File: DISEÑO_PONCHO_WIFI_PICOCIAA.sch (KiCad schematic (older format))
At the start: 11 parts, among them P1 MOUNT_HOLE, P2 MOUNT_HOLE, U1 ESP-12E

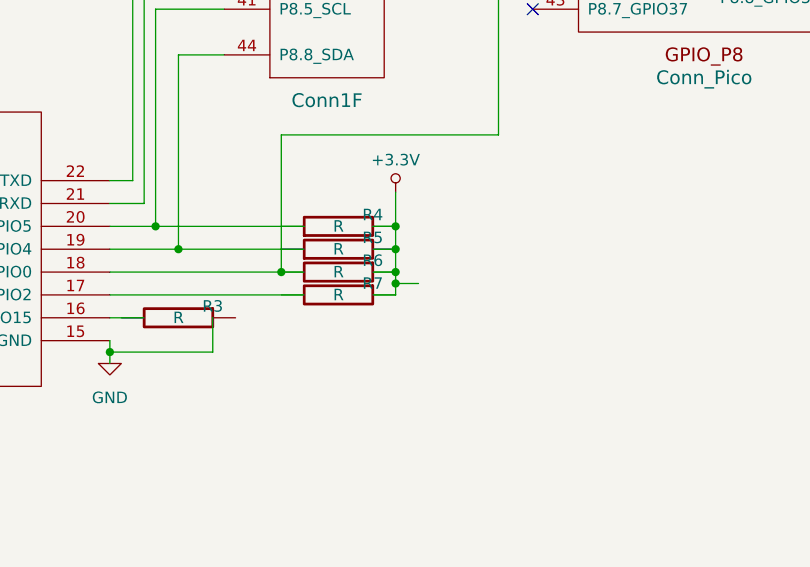
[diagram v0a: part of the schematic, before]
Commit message: Comentarios DB
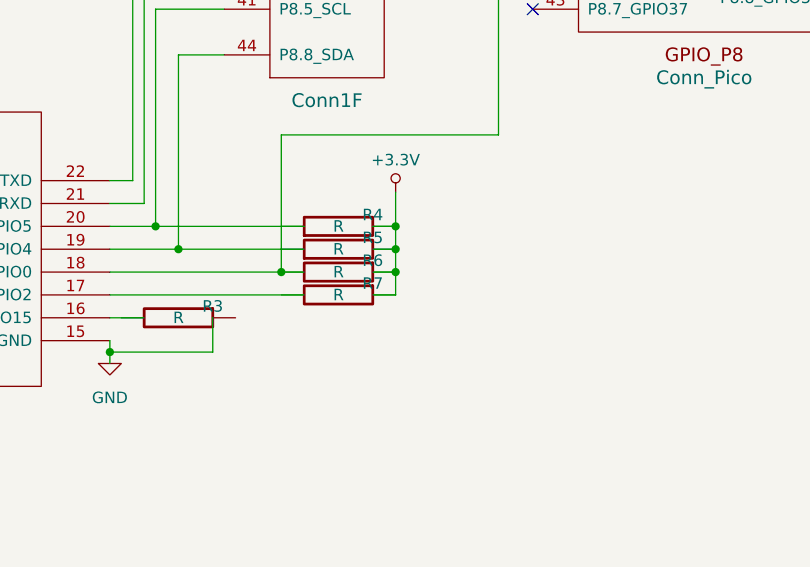
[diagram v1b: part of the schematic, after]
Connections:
- wire segments 52 -> 51
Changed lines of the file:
@@
 EESchema Schematic File Version 2
 LIBS:power
-LIBS:device
-LIBS:transistors
-LIBS:conn
-LIBS:linear
-LIBS:regul
-LIBS:74xx
-LIBS:cmos4000
-LIBS:adc-dac
-LIBS:memory
-LIBS:xilinx
-LIBS:microcontrollers
-LIBS:dsp
-LIBS:microchip
-LIBS:analog_switches
-LIBS:motorola
-LIBS:texas
-LIBS:intel
-LIBS:audio
-LIBS:interface
-LIBS:digital-audio
-LIBS:philips
-LIBS:display
-LIBS:cypress
-LIBS:siliconi
-LIBS:opto
-LIBS:atmel
-LIBS:contrib
-LIBS:valves
-LIBS:ESP8266
-LIBS:logo
-LIBS:poncho_eth
-LIBS:PonchoPLC-cache
-LIBS:Poncho_Esqueleto
 LIBS:DISEÑO_PONCHO_WIFI_PICOCIAA-cache
 EELAYER 25 0
@@
 	7050 4950 6600 4950
 Connection ~ 6600 4950
-Wire Wire Line
-	7850 4650 7950 4650
-Connection ~ 7850 4650
 Connection ~ 6900 4500
 Connection ~ 6800 4400

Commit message: Footprints locales
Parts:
- Conn1: footprint pico_ciaa_ponchos:Conn_Pico_Ciaa -> Poncho_wifi:Conn_Pico_Ciaa
- P1, P2: footprint footprints:PIN_ARRAY_1 -> Poncho_wifi:PIN_ARRAY_1
- R1, R2, R3, R4, R5, R6, R7: footprint Resistors_SMD:R_0805_HandSoldering -> Poncho_wifi:R_0805_HandSoldering
- U1: footprint pico_ciaa_ponchos:ESP-12E -> Poncho_wifi:ESP-12E
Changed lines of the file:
@@
 F 0 "U1" H 5700 4400 50  0000 C CNN
 F 1 "ESP-12E" H 5700 4600 50  0000 C CNN
-F 2 "pico_ciaa_ponchos:ESP-12E" H 5700 4500 50  0001 C CNN
+F 2 "Poncho_wifi:ESP-12E" H 5700 4500 50  0001 C CNN
 F 3 "" H 5700 4500 50  0001 C CNN
 	1    5700 4500
@@
 F 0 "R1" V 4400 4350 50  0000 C CNN
 F 1 "R" V 4450 4200 50  0000 C CNN
-F 2 "Resistors_SMD:R_0805_HandSoldering" V 4380 4200 50  0001 C CNN
+F 2 "Poncho_wifi:R_0805_HandSoldering" V 4380 4200 50  0001 C CNN
 F 3 "" H 4450 4200 50  0000 C CNN
 	1    4450 4200
@@
 F 0 "R2" V 4400 4550 50  0000 C CNN
 F 1 "R" V 4450 4400 50  0000 C CNN
-F 2 "Resistors_SMD:R_0805_HandSoldering" V 4380 4400 50  0001 C CNN
+F 2 "Poncho_wifi:R_0805_HandSoldering" V 4380 4400 50  0001 C CNN
 F 3 "" H 4450 4400 50  0000 C CNN
 	1    4450 4400
@@
 F 0 "R6" V 7550 4750 50  0000 C CNN
 F 1 "R" V 7600 4600 50  0000 C CNN
-F 2 "Resistors_SMD:R_0805_HandSoldering" V 7530 4600 50  0001 C CNN
+F 2 "Poncho_wifi:R_0805_HandSoldering" V 7530 4600 50  0001 C CNN
 F 3 "" H 7600 4600 50  0000 C CNN
 	1    7600 4600
@@
 F 0 "R7" V 7550 4850 50  0000 C CNN
 F 1 "R" V 7600 4700 50  0000 C CNN
-F 2 "Resistors_SMD:R_0805_HandSoldering" V 7530 4700 50  0001 C CNN
+F 2 "Poncho_wifi:R_0805_HandSoldering" V 7530 4700 50  0001 C CNN
 F 3 "" H 7600 4700 50  0000 C CNN
 	1    7600 4700
@@
 F 0 "R3" V 6850 4950 50  0000 C CNN
 F 1 "R" V 6900 4800 50  0000 C CNN
-F 2 "Resistors_SMD:R_0805_HandSoldering" V 6830 4800 50  0001 C CNN
+F 2 "Poncho_wifi:R_0805_HandSoldering" V 6830 4800 50  0001 C CNN
 F 3 "" H 6900 4800 50  0000 C CNN
 	1    6900 4800
@@
 F 0 "R4" V 7650 4250 50  0000 C CNN
 F 1 "R" V 7600 4400 50  0000 C CNN
-F 2 "Resistors_SMD:R_0805_HandSoldering" V 7530 4400 50  0001 C CNN
+F 2 "Poncho_wifi:R_0805_HandSoldering" V 7530 4400 50  0001 C CNN
 F 3 "" H 7600 4400 50  0000 C CNN
 	1    7600 4400
@@
 F 0 "R5" V 7650 4350 50  0000 C CNN
 F 1 "R" V 7600 4500 50  0000 C CNN
-F 2 "Resistors_SMD:R_0805_HandSoldering" V 7530 4500 50  0001 C CNN
+F 2 "Poncho_wifi:R_0805_HandSoldering" V 7530 4500 50  0001 C CNN
 F 3 "" H 7600 4500 50  0000 C CNN
 	1    7600 4500
@@
 F 0 "P1" H 2100 6900 50  0000 C CNN
 F 1 "MOUNT_HOLE" V 2200 6800 50  0000 C CNN
-F 2 "footprints:PIN_ARRAY_1" H 2100 6800 50  0001 C CNN
+F 2 "Poncho_wifi:PIN_ARRAY_1" H 2100 6800 50  0001 C CNN
 F 3 "" H 2100 6800 50  0000 C CNN
 	1    2100 6800
@@
 F 0 "P2" H 2100 7450 50  0000 C CNN
 F 1 "MOUNT_HOLE" V 2200 7350 50  0000 C CNN
-F 2 "footprints:PIN_ARRAY_1" H 2100 7350 50  0001 C CNN
+F 2 "Poncho_wifi:PIN_ARRAY_1" H 2100 7350 50  0001 C CNN
 F 3 "" H 2100 7350 50  0000 C CNN
 	1    2100 7350
@@
 F 0 "Conn1" H 3100 4950 60  0000 C CNN
 F 1 "Conn_Pico" H 3100 3850 60  0000 C CNN
-F 2 "pico_ciaa_ponchos:Conn_Pico_Ciaa" H 3250 4400 60  0001 C CNN
+F 2 "Poncho_wifi:Conn_Pico_Ciaa" H 3250 4400 60  0001 C CNN
 F 3 "" H 3250 4400 60  0000 C CNN
 F 4 "Value" H 3100 4450 60  0001 C CNN "Digikey#"
@@
 F 0 "Conn1" H 7500 2800 60  0000 C CNN
 F 1 "Conn_Pico" H 7500 2000 60  0000 C CNN
-F 2 "pico_ciaa_ponchos:Conn_Pico_Ciaa" H 7500 2400 60  0001 C CNN
+F 2 "Poncho_wifi:Conn_Pico_Ciaa" H 7500 2400 60  0001 C CNN
 F 3 "" H 7500 2400 60  0000 C CNN
 F 4 "Value" H 7500 2450 60  0001 C CNN "Digikey#"
@@
 F 0 "Conn1" H 7550 3850 60  0000 C CNN
 F 1 "Conn_Pico" H 7550 3150 60  0000 C CNN
-F 2 "pico_ciaa_ponchos:Conn_Pico_Ciaa" H 7550 3500 60  0001 C CNN
+F 2 "Poncho_wifi:Conn_Pico_Ciaa" H 7550 3500 60  0001 C CNN
 F 3 "" H 7550 3500 60  0000 C CNN
 F 4 "Value" H 7550 3550 60  0001 C CNN "Digikey#"
@@
 F 0 "Conn1" H 9200 3600 60  0000 C CNN
 F 1 "Conn_Pico" H 9200 2850 60  0000 C CNN
-F 2 "pico_ciaa_ponchos:Conn_Pico_Ciaa" H 9200 3250 60  0001 C CNN
+F 2 "Poncho_wifi:Conn_Pico_Ciaa" H 9200 3250 60  0001 C CNN
 F 3 "" H 9200 3250 60  0000 C CNN
 F 4 "Value" H 9200 3300 60  0001 C CNN "Digikey#"
@@
 F 0 "Conn1" H 1350 2150 60  0000 C CNN
 F 1 "Conn_Pico" H 1300 1350 60  0000 C CNN
-F 2 "pico_ciaa_ponchos:Conn_Pico_Ciaa" H 1350 1800 60  0001 C CNN
+F 2 "Poncho_wifi:Conn_Pico_Ciaa" H 1350 1800 60  0001 C CNN
 F 3 "" H 1350 1800 60  0000 C CNN
 F 4 "Value" H 1350 1850 60  0001 C CNN "Digikey#"

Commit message: Ruteo y limpieza de proyecto
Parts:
- added FID1, FID2, FID3: FIDUCIAL, Poncho_wifi:Fiducial_1mm_Dia_2.54mm_Outer_CopperTop, symbol FIDUCIAL
- R1, R2, R3, R4, R5, R6, R7: Digikey# (none) -> 1056-MCR10J103-CHP
- U1: Digikey# (none) -> 1528-1438-ND
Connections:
- wire segments 51 -> 47
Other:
- moved on the sheet: R3
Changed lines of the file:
@@
 EESchema Schematic File Version 2
-LIBS:power
+LIBS:poncho_eth
 LIBS:DISEÑO_PONCHO_WIFI_PICOCIAA-cache
 EELAYER 25 0
@@
 F 2 "Poncho_wifi:ESP-12E" H 5700 4500 50  0001 C CNN
 F 3 "" H 5700 4500 50  0001 C CNN
+F 4 "1528-1438-ND" H 5700 4500 60  0001 C CNN "Digikey#"
 	1    5700 4500
 	1    0    0    -1
@@
 F 2 "Poncho_wifi:R_0805_HandSoldering" V 4380 4200 50  0001 C CNN
 F 3 "" H 4450 4200 50  0000 C CNN
+F 4 "1056-MCR10J103-CHP" H 4450 4200 60  0001 C CNN "Digikey#"
 	1    4450 4200
 	0    1    1    0
@@
 F 2 "Poncho_wifi:R_0805_HandSoldering" V 4380 4400 50  0001 C CNN
 F 3 "" H 4450 4400 50  0000 C CNN
+F 4 "1056-MCR10J103-CHP" H 4450 4400 60  0001 C CNN "Digikey#"
 	1    4450 4400
 	0    1    1    0
@@
 F 2 "Poncho_wifi:R_0805_HandSoldering" V 7530 4600 50  0001 C CNN
 F 3 "" H 7600 4600 50  0000 C CNN
+F 4 "1056-MCR10J103-CHP" H 7600 4600 60  0001 C CNN "Digikey#"
 	1    7600 4600
 	0    1    1    0
@@
 F 2 "Poncho_wifi:R_0805_HandSoldering" V 7530 4700 50  0001 C CNN
 F 3 "" H 7600 4700 50  0000 C CNN
+F 4 "1056-MCR10J103-CHP" H 7600 4700 60  0001 C CNN "Digikey#"
 	1    7600 4700
 	0    1    1    0
@@
 L R R3
 U 1 1 58264232
-P 6900 4800
-F 0 "R3" V 6850 4950 50  0000 C CNN
-F 1 "R" V 6900 4800 50  0000 C CNN
-F 2 "Poncho_wifi:R_0805_HandSoldering" V 6830 4800 50  0001 C CNN
-F 3 "" H 6900 4800 50  0000 C CNN
-	1    6900 4800
+P 7000 4800
+F 0 "R3" V 6950 4950 50  0000 C CNN
+F 1 "R" V 7000 4800 50  0000 C CNN
+F 2 "Poncho_wifi:R_0805_HandSoldering" V 6930 4800 50  0001 C CNN
+F 3 "" H 7000 4800 50  0000 C CNN
+F 4 "1056-MCR10J103-CHP" H 7000 4800 60  0001 C CNN "Digikey#"
+	1    7000 4800
 	0    1    1    0
 $EndComp
@@
 F 2 "Poncho_wifi:R_0805_HandSoldering" V 7530 4400 50  0001 C CNN
 F 3 "" H 7600 4400 50  0000 C CNN
+F 4 "1056-MCR10J103-CHP" H 7600 4400 60  0001 C CNN "Digikey#"
 	1    7600 4400
 	0    -1   -1   0
@@
 F 2 "Poncho_wifi:R_0805_HandSoldering" V 7530 4500 50  0001 C CNN
 F 3 "" H 7600 4500 50  0000 C CNN
+F 4 "1056-MCR10J103-CHP" H 7600 4500 60  0001 C CNN "Digikey#"
 	1    7600 4500
 	0    -1   -1   0
 $EndComp
-Wire Wire Line
-	6600 4400 7450 4400
-Wire Wire Line
-	6600 4500 7450 4500
-Wire Wire Line
-	6600 4600 7450 4600
-Wire Wire Line
-	6600 4700 7450 4700
-Wire Wire Line
-	6600 4800 6750 4800
-Wire Wire Line
-	6600 4900 6600 5000
-Wire Wire Line
-	4800 4900 4800 5050
-Wire Wire Line
-	4800 5050 4500 5050
-Wire Wire Line
-	4500 5050 4500 5000
-Wire Wire Line
-	4800 4200 4600 4200
-Wire Wire Line
-	4800 4400 4600 4400
-Wire Wire Line
-	4150 4050 4150 4400
-Wire Wire Line
-	4150 4400 4300 4400
-Wire Wire Line
-	4300 4200 4150 4200
-Connection ~ 4150 4200
-Wire Wire Line
-	7050 4800 7050 4950
-Wire Wire Line
-	7050 4950 6600 4950
-Connection ~ 6600 4950
-Connection ~ 6900 4500
-Connection ~ 6800 4400
-Wire Wire Line
-	7850 4700 7750 4700
-Wire Wire Line
-	7850 4250 7850 4700
-Wire Wire Line
-	7750 4600 7850 4600
-Wire Wire Line
-	7750 4500 7850 4500
-Connection ~ 7850 4600
-Wire Wire Line
-	7750 4400 7850 4400
-Connection ~ 7850 4500
-Connection ~ 7850 4400
-Connection ~ 7350 4600
 $Comp
 L +3.3V #PWR05
@@
 	1    0    0    -1
 $EndComp
-Wire Wire Line
-	1500 1150 1500 1350
 $Comp
 L GND #PWR06
@@
 	1    0    0    -1
 $EndComp
-Wire Wire Line
-	1000 1200 1000 1100
-Wire Wire Line
-	1000 1100 1200 1100
-Wire Wire Line
-	1200 1100 1200 1350
 $Comp
 L Logo_Poncho #G2
@@
 	1    0    0    -1
 $EndComp
-Wire Wire Line
-	1900 6800 1750 6800
-Wire Wire Line
-	1750 6800 1750 7350
-Wire Wire Line
-	1750 7350 1900 7350
-Wire Wire Line
-	1600 7100 1600 7050
-Wire Wire Line
-	1550 7050 1750 7050
-Connection ~ 1750 7050
 $Comp
 L PWR_FLAG #FLG08
@@
 	1    0    0    -1
 $EndComp
-Wire Wire Line
-	1550 6950 1550 7050
-Connection ~ 1600 7050
 $Comp
 L PWR_FLAG #FLG09
@@
 	1    0    0    -1
 $EndComp
-Wire Wire Line
-	1800 1100 1800 1200
-Wire Wire Line
-	1800 1200 1500 1200
-Connection ~ 1500 1200
 $Comp
 L Conn_Pico_Ciaa_Esqueleto Conn1
@@
 	1    0    0    -1
 $EndComp
-Wire Wire Line
-	4800 4800 4550 4800
-Wire Wire Line
-	4550 4800 4550 4750
-Wire Wire Line
-	4550 4750 3900 4750
 NoConn ~ 3900 4650
 NoConn ~ 3900 4550
@@
 	-1   0    0    -1
 $EndComp
-Wire Wire Line
-	6600 4200 6700 4200
-Wire Wire Line
-	6700 4200 6700 2350
-Wire Wire Line
-	6600 4300 6750 4300
-Wire Wire Line
-	6750 4300 6750 2550
-Wire Wire Line
-	6750 2550 6850 2550
-Wire Wire Line
-	6700 2350 6850 2350
 NoConn ~ 8150 2300
 NoConn ~ 8150 2450
@@
 	-1   0    0    1
 $EndComp
-Wire Wire Line
-	6900 4500 6900 3650
-Wire Wire Line
-	6900 3650 7100 3650
-Wire Wire Line
-	6800 4400 6800 3450
-Wire Wire Line
-	6800 3450 7100 3450
 $Comp
 L Conn_Pico_Ciaa_Esqueleto Conn1
@@
 	1    0    0    -1
 $EndComp
-Wire Wire Line
-	7350 4600 7350 4000
-Wire Wire Line
-	7350 4000 8300 4000
-Wire Wire Line
-	8300 4000 8300 3250
-Wire Wire Line
-	8300 3250 8450 3250
 NoConn ~ 8450 3150
 NoConn ~ 8450 3350
@@
 	0    1    -1   0
 $EndComp
+$Comp
+L FIDUCIAL FID1
+U 1 1 585874B1
+P 4500 7050
+F 0 "FID1" H 4500 7175 60  0000 C CNN
+F 1 "FIDUCIAL" H 4500 6925 60  0000 C CNN
+F 2 "Poncho_wifi:Fiducial_1mm_Dia_2.54mm_Outer_CopperTop" H 4500 7050 60  0001 C CNN
+F 3 "" H 4500 7050 60  0000 C CNN
+	1    4500 7050
+	1    0    0    -1
+$EndComp
+$Comp
+L FIDUCIAL FID2
+U 1 1 58587594
+P 4950 7050
+F 0 "FID2" H 4950 7175 60  0000 C CNN
+F 1 "FIDUCIAL" H 4950 6925 60  0000 C CNN
+F 2 "Poncho_wifi:Fiducial_1mm_Dia_2.54mm_Outer_CopperTop" H 4950 7050 60  0001 C CNN
+F 3 "" H 4950 7050 60  0000 C CNN
+	1    4950 7050
+	1    0    0    -1
+$EndComp
+$Comp
+L FIDUCIAL FID3
+U 1 1 58587609
+P 5400 7050
+F 0 "FID3" H 5400 7175 60  0000 C CNN
+F 1 "FIDUCIAL" H 5400 6925 60  0000 C CNN
+F 2 "Poncho_wifi:Fiducial_1mm_Dia_2.54mm_Outer_CopperTop" H 5400 7050 60  0001 C CNN
+F 3 "" H 5400 7050 60  0000 C CNN
+	1    5400 7050
+	1    0    0    -1
+$EndComp
+Wire Wire Line
+	6600 4800 6750 4800
+Wire Wire Line
+	6600 4900 6600 5000
+Wire Wire Line
+	4800 4900 4800 5050
+Wire Wire Line
+	4800 5050 4500 5050
+Wire Wire Line
+	4500 5050 4500 5000
+Wire Wire Line
+	4150 4050 4150 4400
+Connection ~ 4150 4200
+Wire Wire Line
+	7250 4800 7250 4950
+Wire Wire Line
+	7250 4950 6600 4950
+Connection ~ 6600 4950
+Connection ~ 6900 4500
+Connection ~ 6800 4400
+Connection ~ 7250 4600
+Wire Wire Line
+	1500 1150 1500 1350
+Wire Wire Line
+	1000 1200 1000 1100
+Wire Wire Line
+	1000 1100 1200 1100
+Wire Wire Line
+	1200 1100 1200 1350
+Wire Wire Line
+	1900 6800 1750 6800
+Wire Wire Line
+	1750 6800 1750 7350
+Wire Wire Line
+	1750 7350 1900 7350
+Wire Wire Line
+	1600 7100 1600 7050
+Wire Wire Line
+	1550 7050 1750 7050
+Connection ~ 1750 7050
+Wire Wire Line
+	1550 6950 1550 7050
+Connection ~ 1600 7050
+Wire Wire Line
+	1800 1100 1800 1200
+Wire Wire Line
+	1800 1200 1500 1200
+Connection ~ 1500 1200
+Wire Wire Line
+	4800 4800 4550 4800
+Wire Wire Line
+	4550 4800 4550 4750
+Wire Wire Line
+	4550 4750 3900 4750
+Wire Wire Line
+	6600 4200 6700 4200
+Wire Wire Line
+	6700 4200 6700 2350
+Wire Wire Line
+	6600 4300 6750 4300
+Wire Wire Line
+	6750 4300 6750 2550
+Wire Wire Line
+	6750 2550 6850 2550
+Wire Wire Line
+	6700 2350 6850 2350
+Wire Wire Line
+	6900 4500 6900 3650
+Wire Wire Line
+	6900 3650 7100 3650
+Wire Wire Line
+	6800 4400 6800 3450
+Wire Wire Line
+	6800 3450 7100 3450
+Wire Wire Line
+	7250 4600 7250 4000
+Wire Wire Line
+	7250 4000 8300 4000
+Wire Wire Line
+	8300 4000 8300 3250
+Wire Wire Line
+	8300 3250 8450 3250
 Wire Wire Line
 	1200 1350 1350 1350
 Connection ~ 1200 1350
+Wire Wire Line
+	4700 4200 4800 4200
+Wire Wire Line
+	4700 4400 4800 4400
+Wire Wire Line
+	4150 4200 4200 4200
+Wire Wire Line
+	4150 4400 4200 4400
+Wire Wire Line
+	6600 4400 7350 4400
+Wire Wire Line
+	7850 4250 7850 4700
+Connection ~ 7850 4600
+Connection ~ 7850 4500
+Connection ~ 7850 4400
+Wire Wire Line
+	6600 4600 7350 4600
+Wire Wire Line
+	6600 4500 7350 4500
+Wire Wire Line
+	7350 4700 6600 4700
 $EndSCHEMATC

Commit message: Ruteo y limpoeza del proyecto
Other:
- moved on the sheet: FID1, FID2, FID3
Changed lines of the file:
@@
 Rev "V1.0"
 Comp "FIUBA"
-Comment1 "Diseñado por: Sergio De Jesús"
-Comment2 "Licencias en: LICENCIA_Y_COLABORADORES/LICENSE"
-Comment3 ""
+Comment1 "Revisor: Sebastián López"
+Comment2 "Diseñado por: Sergio De Jesús"
+Comment3 "Licencias en: LICENCIA_Y_COLABORADORES/LICENSE"
 Comment4 ""
 $EndDescr
@@
 F 3 "" H 1000 1200 50  0000 C CNN
 	1    1000 1200
-	1    0    0    -1
-$EndComp
-$Comp
-L Logo_Poncho #G2
-U 1 1 5838FBE9
-P 3750 6900
-F 0 "#G2" H 3700 6500 60  0001 C CNN
-F 1 "Logo_Poncho" H 3950 6500 60  0001 C CNN
-F 2 "" H 3750 6900 60  0000 C CNN
-F 3 "" H 3750 6900 60  0000 C CNN
-	1    3750 6900
 	1    0    0    -1
 $EndComp
@@
 L FIDUCIAL FID1
 U 1 1 585874B1
-P 4500 7050
-F 0 "FID1" H 4500 7175 60  0000 C CNN
-F 1 "FIDUCIAL" H 4500 6925 60  0000 C CNN
-F 2 "Poncho_wifi:Fiducial_1mm_Dia_2.54mm_Outer_CopperTop" H 4500 7050 60  0001 C CNN
-F 3 "" H 4500 7050 60  0000 C CNN
-	1    4500 7050
+P 3700 7100
+F 0 "FID1" H 3700 7225 60  0000 C CNN
+F 1 "FIDUCIAL" H 3700 6975 60  0000 C CNN
+F 2 "Poncho_wifi:Fiducial_1mm_Dia_2.54mm_Outer_CopperTop" H 3700 7100 60  0001 C CNN
+F 3 "" H 3700 7100 60  0000 C CNN
+	1    3700 7100
 	1    0    0    -1
 $EndComp
@@
 L FIDUCIAL FID2
 U 1 1 58587594
-P 4950 7050
-F 0 "FID2" H 4950 7175 60  0000 C CNN
-F 1 "FIDUCIAL" H 4950 6925 60  0000 C CNN
-F 2 "Poncho_wifi:Fiducial_1mm_Dia_2.54mm_Outer_CopperTop" H 4950 7050 60  0001 C CNN
-F 3 "" H 4950 7050 60  0000 C CNN
-	1    4950 7050
+P 4150 7100
+F 0 "FID2" H 4150 7225 60  0000 C CNN
+F 1 "FIDUCIAL" H 4150 6975 60  0000 C CNN
+F 2 "Poncho_wifi:Fiducial_1mm_Dia_2.54mm_Outer_CopperTop" H 4150 7100 60  0001 C CNN
+F 3 "" H 4150 7100 60  0000 C CNN
+	1    4150 7100
 	1    0    0    -1
 $EndComp
@@
 L FIDUCIAL FID3
 U 1 1 58587609
-P 5400 7050
-F 0 "FID3" H 5400 7175 60  0000 C CNN
-F 1 "FIDUCIAL" H 5400 6925 60  0000 C CNN
-F 2 "Poncho_wifi:Fiducial_1mm_Dia_2.54mm_Outer_CopperTop" H 5400 7050 60  0001 C CNN
-F 3 "" H 5400 7050 60  0000 C CNN
-	1    5400 7050
-	1    0    0    -1
-$EndComp
+P 4600 7100
+F 0 "FID3" H 4600 7225 60  0000 C CNN
+F 1 "FIDUCIAL" H 4600 6975 60  0000 C CNN
+F 2 "Poncho_wifi:Fiducial_1mm_Dia_2.54mm_Outer_CopperTop" H 4600 7100 60  0001 C CNN
+F 3 "" H 4600 7100 60  0000 C CNN
+	1    4600 7100
+	1    0    0    -1
+$EndComp
